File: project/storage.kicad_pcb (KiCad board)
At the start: 6 copper layers, 190 x 134 mm, 29 parts

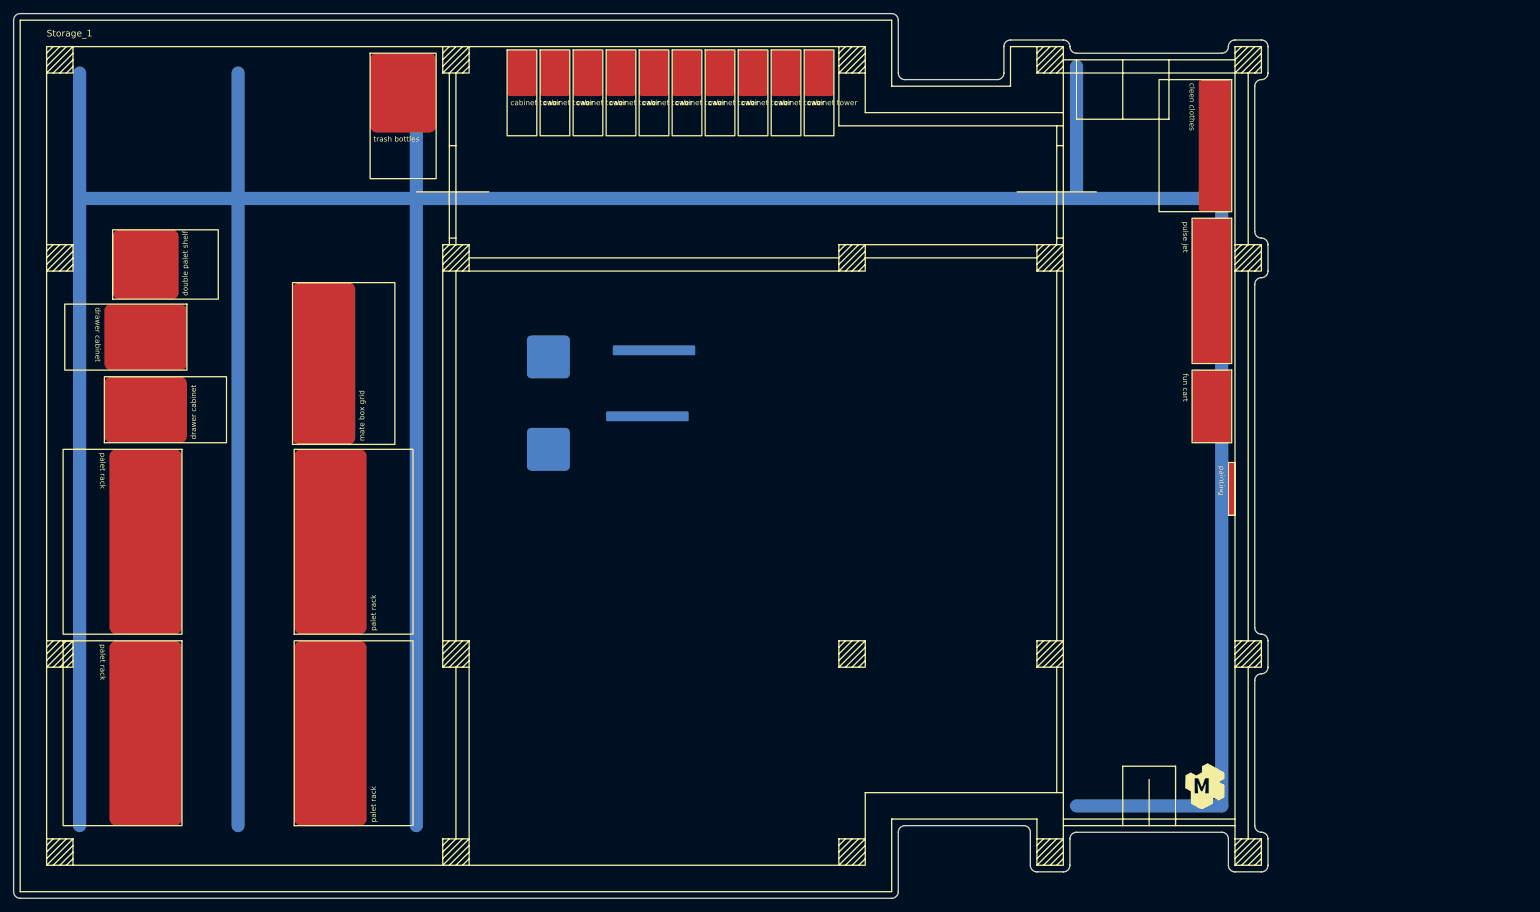
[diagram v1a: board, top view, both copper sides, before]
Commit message: alternate placement for dirty workshop
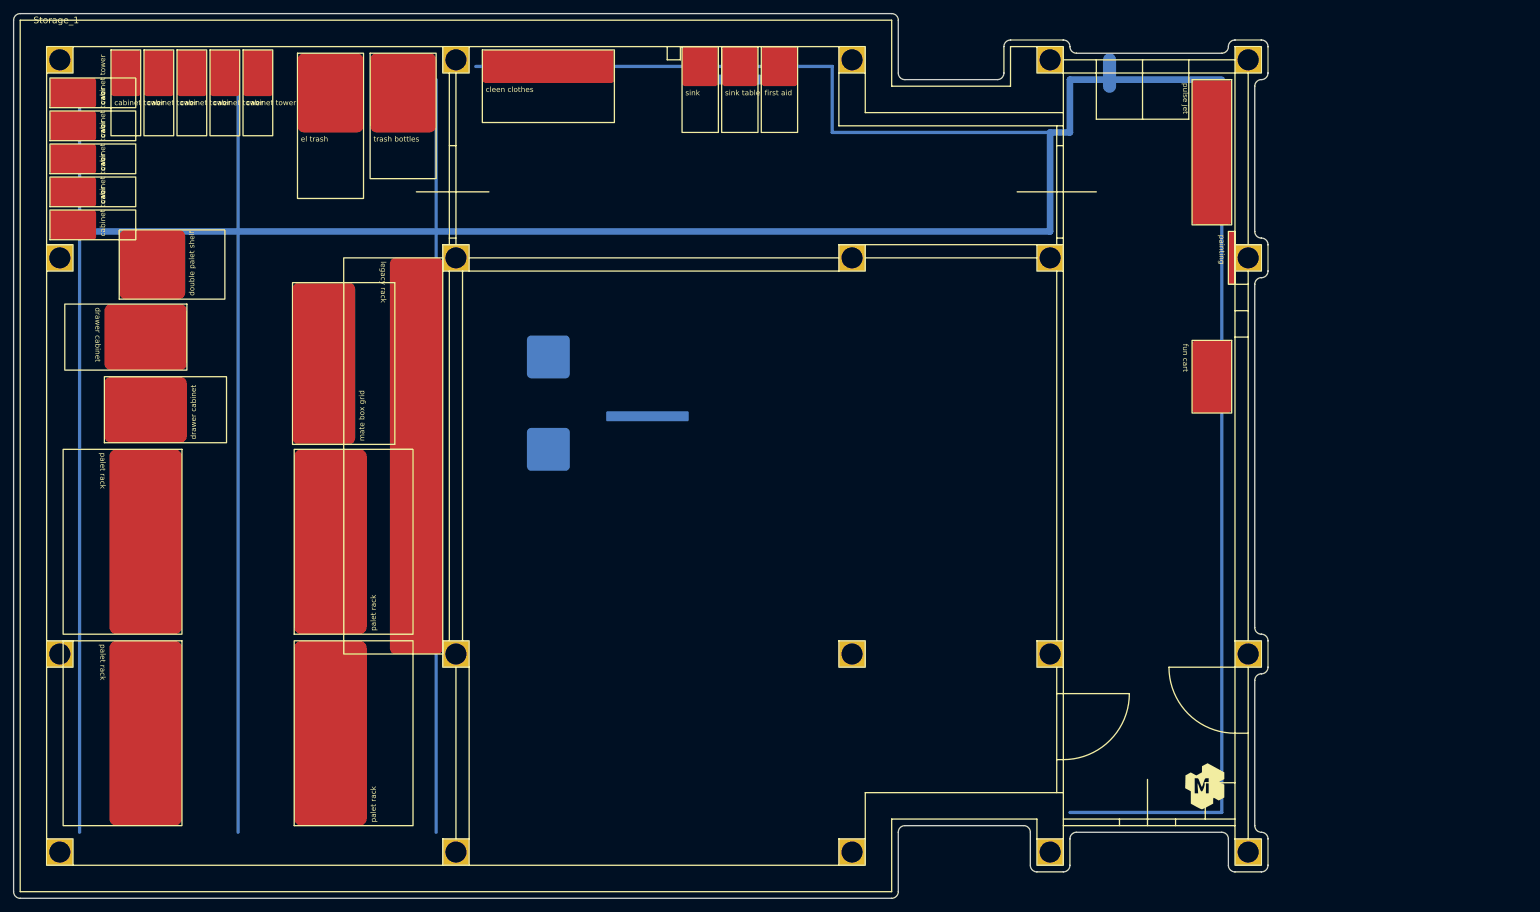
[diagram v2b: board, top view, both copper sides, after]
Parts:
- added R20: legacy rack, -local:_s_legacy_rack__, F.Cu at (115.0, 63.0)
- added R22: el trash, -local:_o_cube_container_x2__, F.Cu at (93.0, 32.0)
- added R23: sink, -local:_s_sink__, F.Cu at (151.2, 31.0)
- added R24: sink table, -local:_s_sink_table__, F.Cu at (157.2, 31.0)
- added R25: first aid, -local:_s_first_aid__, F.Cu at (163.2, 31.0)
- moved R21 113.6 mm to (121.0, 31.5), turned to 0 degrees
- moved R14 89.7 mm to (55.5, 40.2), turned to 90 degrees
- moved R13 85.4 mm to (55.5, 45.2), turned to 90 degrees
- moved R15 85.0 mm to (64.8, 31.5)
- moved R16 85.0 mm to (69.8, 31.5)
- moved R17 85.0 mm to (74.8, 31.5)
- moved R18 85.0 mm to (79.8, 31.5)
- moved R19 85.0 mm to (84.8, 31.5)
- moved R12 81.4 mm to (55.5, 50.2), turned to 90 degrees
- moved R11 78.0 mm to (55.5, 55.2), turned to 90 degrees
- moved R10 75.0 mm to (55.5, 60.2), turned to 90 degrees
- moved L3 43.3 mm to (161.0, 36.0)
- moved R28 35.0 mm to (235.0, 59.0)
- moved R26 21.0 mm to (234.5, 36.0)
- moved R27 4.50 mm to (234.5, 75.5)
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- renumbered R15 to R1, R5 to R10, R6 to R11, R7 to R12, R8 to R13, R9 to R14, R10 to R15, R11 to R16, R12 to R17, R13 to R18, R14 to R19, R16 to R2, R1 to R21, R2 to R26, R3 to R27, R4 to R28, R17 to R3, R18 to R4, R19 to R5, R20 to R6, R21 to R7, R22 to R8, R23 to R9
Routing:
- net (no net): track 971.2 -> 322.2 mm

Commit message: adding power cable runs
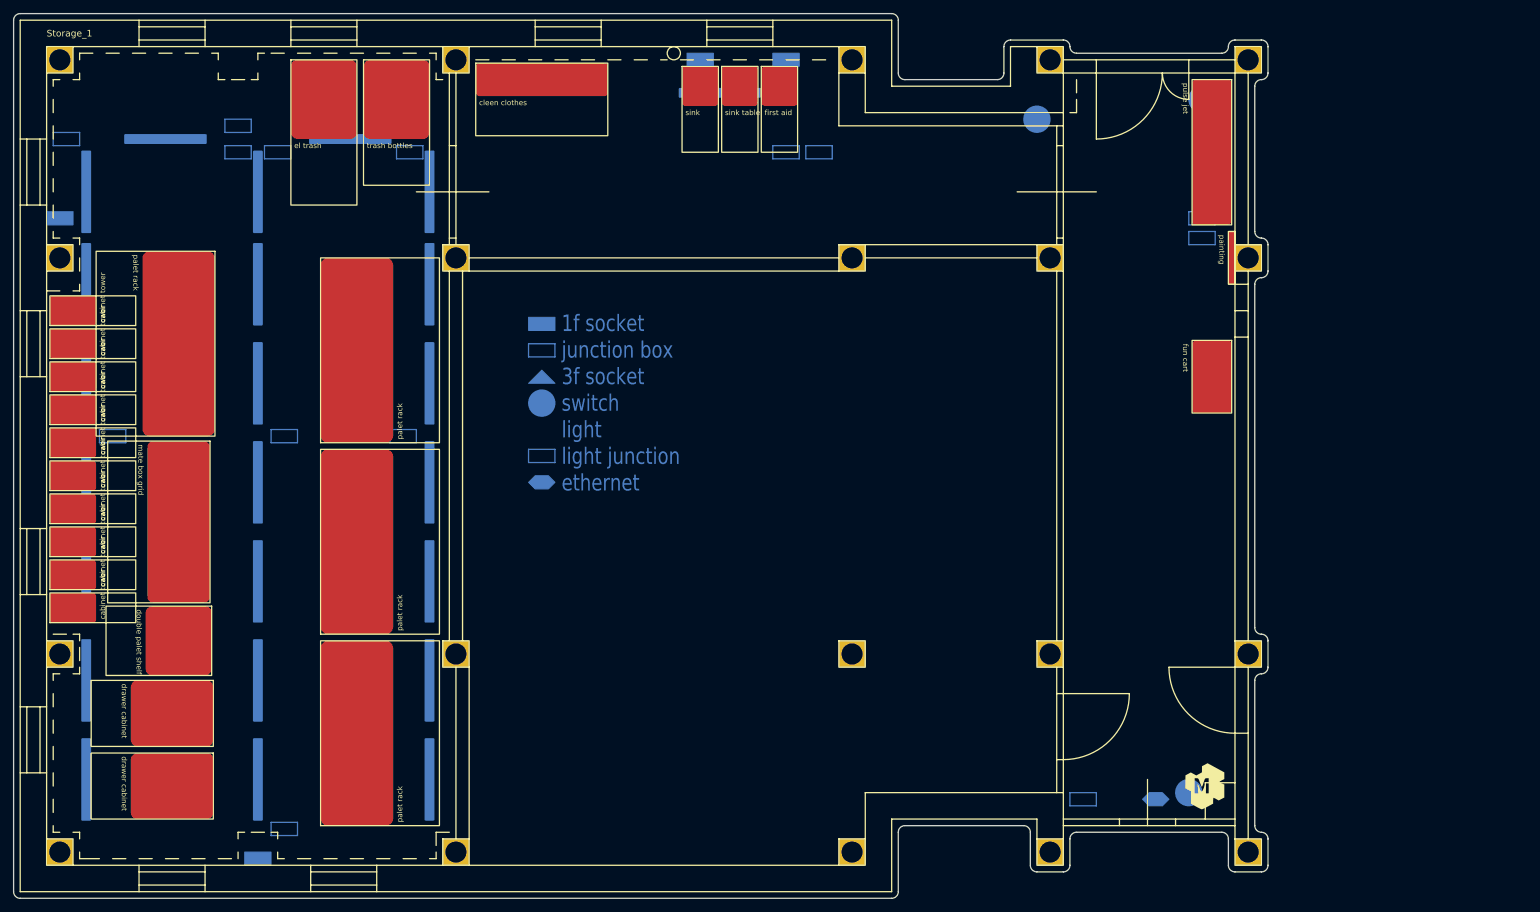
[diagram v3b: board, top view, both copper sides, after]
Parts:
- removed the L1 at (131.0, 78.0)
- removed the L2 at (131.0, 92.0)
- removed the R20 at (115.0, 63.0)
- added L10: light, -local:light_long, B.Cu at (87.0, 127.0)
- added L11: light, -local:light_long, B.Cu at (87.0, 112.0)
- added L12: light, -local:light_long, B.Cu at (87.0, 97.0)
- added L13: light, -local:light_long, B.Cu at (87.0, 82.0)
- added L14: light, -local:light_long, B.Cu at (87.0, 67.0)
- added L15: light, -local:light_long, B.Cu at (87.0, 53.0)
- added L16: light, -local:light_long, B.Cu at (113.0, 142.0)
- added L17: light, -local:light_long, B.Cu at (113.0, 127.0)
- added L18: light, -local:light_long, B.Cu at (113.0, 112.0)
- added L19: light, -local:light_long, B.Cu at (113.0, 97.0)
- added L20: light, -local:light_long, B.Cu at (113.0, 82.0)
- added L21: light, -local:light_long, B.Cu at (113.0, 67.0)
- added L22: light, -local:light_long, B.Cu at (113.0, 53.0)
- added L23: light, -local:light_long, B.Cu at (101.0, 45.0)
- added L24: light, -local:light_long, B.Cu at (157.0, 38.0)
- added L3: light, -local:light_long, B.Cu at (61.0, 112.0)
- added L4: light, -local:light_long, B.Cu at (61.0, 97.0)
- added L5: light, -local:light_long, B.Cu at (61.0, 82.0)
- added L6: light, -local:light_long, B.Cu at (61.0, 67.0)
- added L7: light, -local:light_long, B.Cu at (61.0, 53.0)
- added L8: light, -local:light_long, B.Cu at (73.0, 45.0)
- added L9: light, -local:light_long, B.Cu at (87.0, 142.0)
- moved L1 145.7 mm to (61.0, 142.0), turned to -90 degrees
- moved L2 93.9 mm to (61.0, 127.0), turned to 90 degrees
- moved R15 62.4 mm to (55.5, 93.2), turned to 90 degrees
- moved R2 59.2 mm to (80.5, 62.0)
- moved R16 58.5 mm to (55.5, 88.2), turned to 90 degrees
- moved R10 58.0 mm to (55.5, 118.2)
- moved R11 58.0 mm to (55.5, 113.2)
- moved R12 58.0 mm to (55.5, 108.2)
- moved R13 58.0 mm to (55.5, 103.2)
- moved R14 58.0 mm to (55.5, 98.2)
- moved R8 57.1 mm to (80.2, 127.0)
- moved R17 55.2 mm to (55.5, 83.2), turned to 90 degrees
- moved R18 52.7 mm to (55.5, 78.2), turned to 90 degrees
- moved R19 51.0 mm to (55.5, 73.2), turned to 90 degrees
- moved R9 49.8 mm to (80.2, 138.0), turned to -90 degrees
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- renumbered L3 to L1, L4 to L2, R21 to R20, R22 to R21, R23 to R22, R24 to R23, R25 to R24, R26 to R25, R27 to R26, R28 to R27
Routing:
- net (no net): track 322.2 -> 343.3 mm
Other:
- board text added: "10"
- board text added: "101"
- board text added: "13"
- board text added: "14"
- board text added: "1f socket junction box 3f socket switch light light junction ethernet"
- board text added: "20"
- board text added: "21"
- board text added: "22"
- board text added: "23"
- board text added: "24"
- board text added: "26"
- board text added: "27"
- board text added: "29"
- board text added: "33"
- board text added: "34"
- board text added: "35"
- board text added: "37"
- board text added: "38m"
- board text added: "39"
- board text added: "3x1 13m via P621 sens x1"
- board text added: "3x1 13m via P821 sens x1"
- board text added: "3x1 B2 14m sens x1"
- board text added: "3x1 B2 15m sens x1"
- board text added: "3x1 B2 25m sens x1"
- board text added: "3x2.5 15m via D821 x4"
- board text added: "3x2.5 8m via D821 x4"
- board text added: "3x2.5 C16 32m x6"
- board text added: "3x2.5 C16 38m"
- board text added: "3x2.5 C2 35m pump x2"
- board text added: "40"
- board text added: "42"
- board text added: "45"
- board text added: "48"
- board text added: "51"
- board text added: "7x0.75 B2 26m"
- board text added: "7x0.75 B2 27m"
- board text added: "7x0.75 B2 28m D751"
- board text added: "7x0.75 B2 35m D85L~D85N"
- board text added: "7x0.75 B2 38m D85D~D85G"
- board text added: "7x0.75 B2 40m D85H~D85K"
- board text added: "7x0.75 B2 41m D855~D858"
- board text added: "7x0.75 B2 43m D859~D85C"
- board text added: "7x0.75 B2 46m D851~D854"
- board text added: "8"
- board text added: "9"
- board text added: "D641"
- board text added: "D661"
- board text added: "D711"
- board text added: "D741"
- board text added: "D751"
- board text added: "D761"
- board text added: "D811"
- board text added: "D812"
- board text added: "D821"
- board text added: "D851"
- board text added: "D852"
- board text added: "D853"
- board text added: "D854"
- board text added: "D855"
- board text added: "D856"
- board text added: "D857"
- board text added: "D858"
- board text added: "D859"
- board text added: "D85A"
- board text added: "D85B"
- board text added: "D85C"
- board text added: "D85D"
- board text added: "D85E"
- board text added: "D85F"
- board text added: "D85G"
- board text added: "D85H"
- board text added: "D85I"
- board text added: "D85J"
- board text added: "D85K"
- board text added: "D85L"
- board text added: "D85M"
- board text added: "D85N"
- board text added: "D861"
- board text added: "D862"
- board text added: "D863"
- board text added: "D864"
- board text added: "D865"
- board text added: "D866"
- board text added: "P621"
- board text added: "P622"
- board text added: "P641"
- board text added: "P711"
- board text added: "P721"
- board text added: "P821"
- board text added: "P822"
- board text added: "[source] [room] [type] [number]"
- board text added: "xx1x"
- board text added: "xx2x"
- board text added: "xx3x"
- board text added: "xx4x"
- board text added: "xx5x"
- board text added: "xx6x"
- board text added: "xxx"
